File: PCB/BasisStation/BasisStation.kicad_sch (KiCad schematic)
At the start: 1 part, among them U1 ESP32-S3-WROOM-1-N16R8

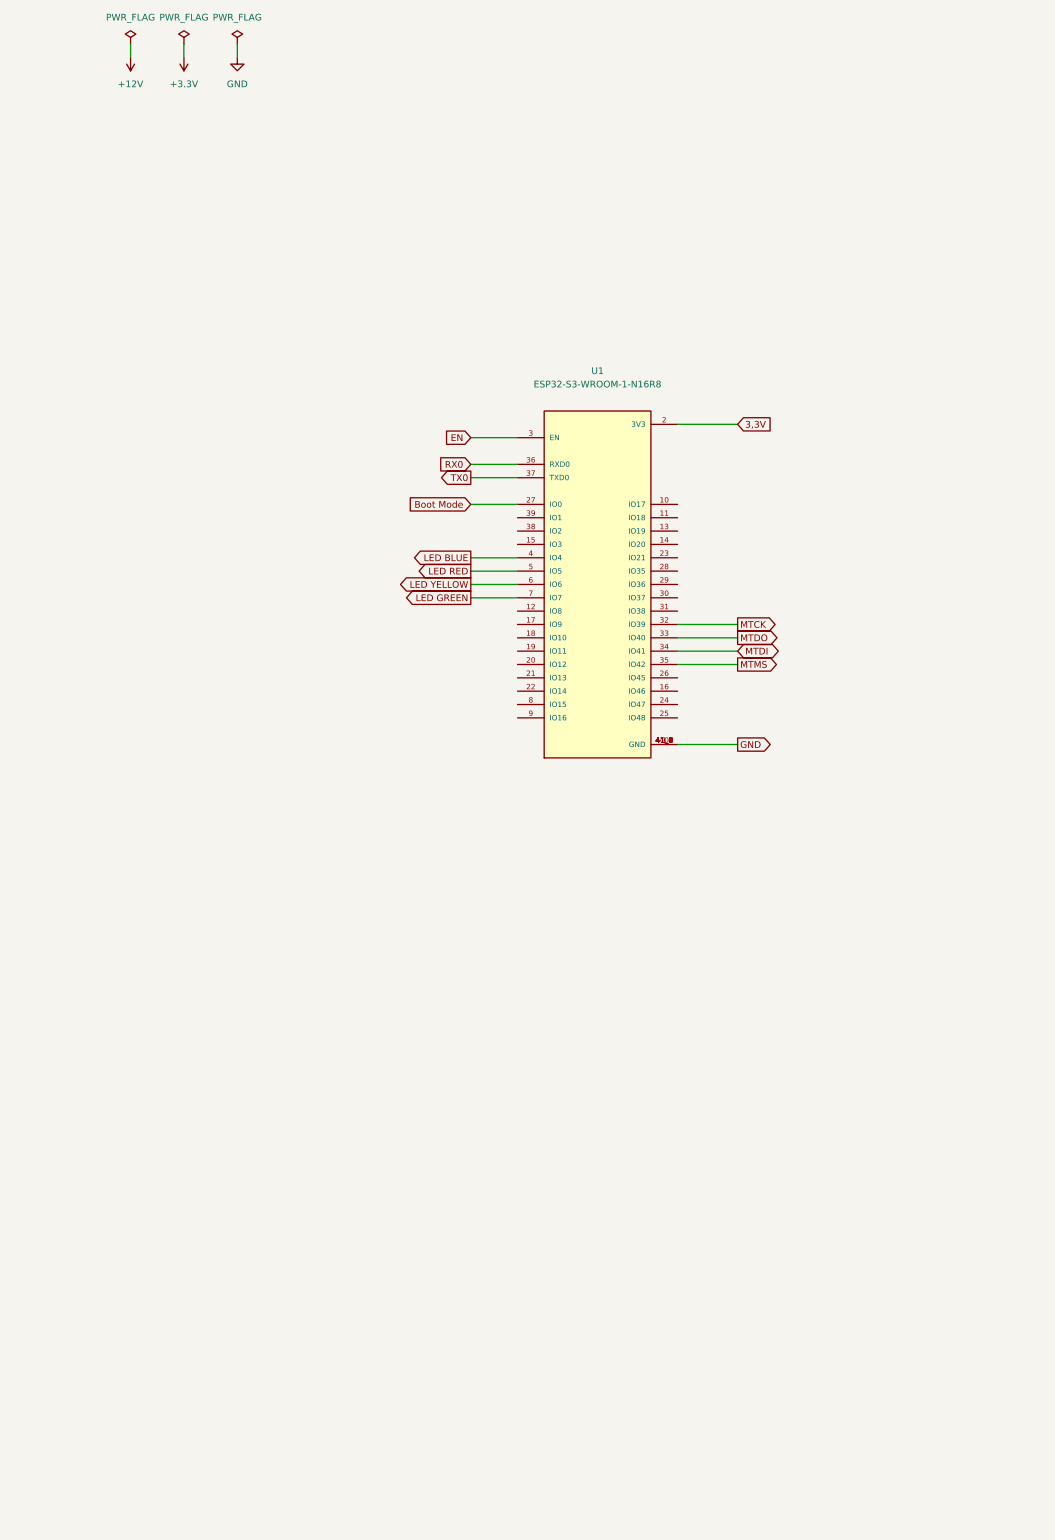
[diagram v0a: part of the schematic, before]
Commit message: ESP32-S3 von der Espressif Library hinzugefügt und Schaltplan angepasst
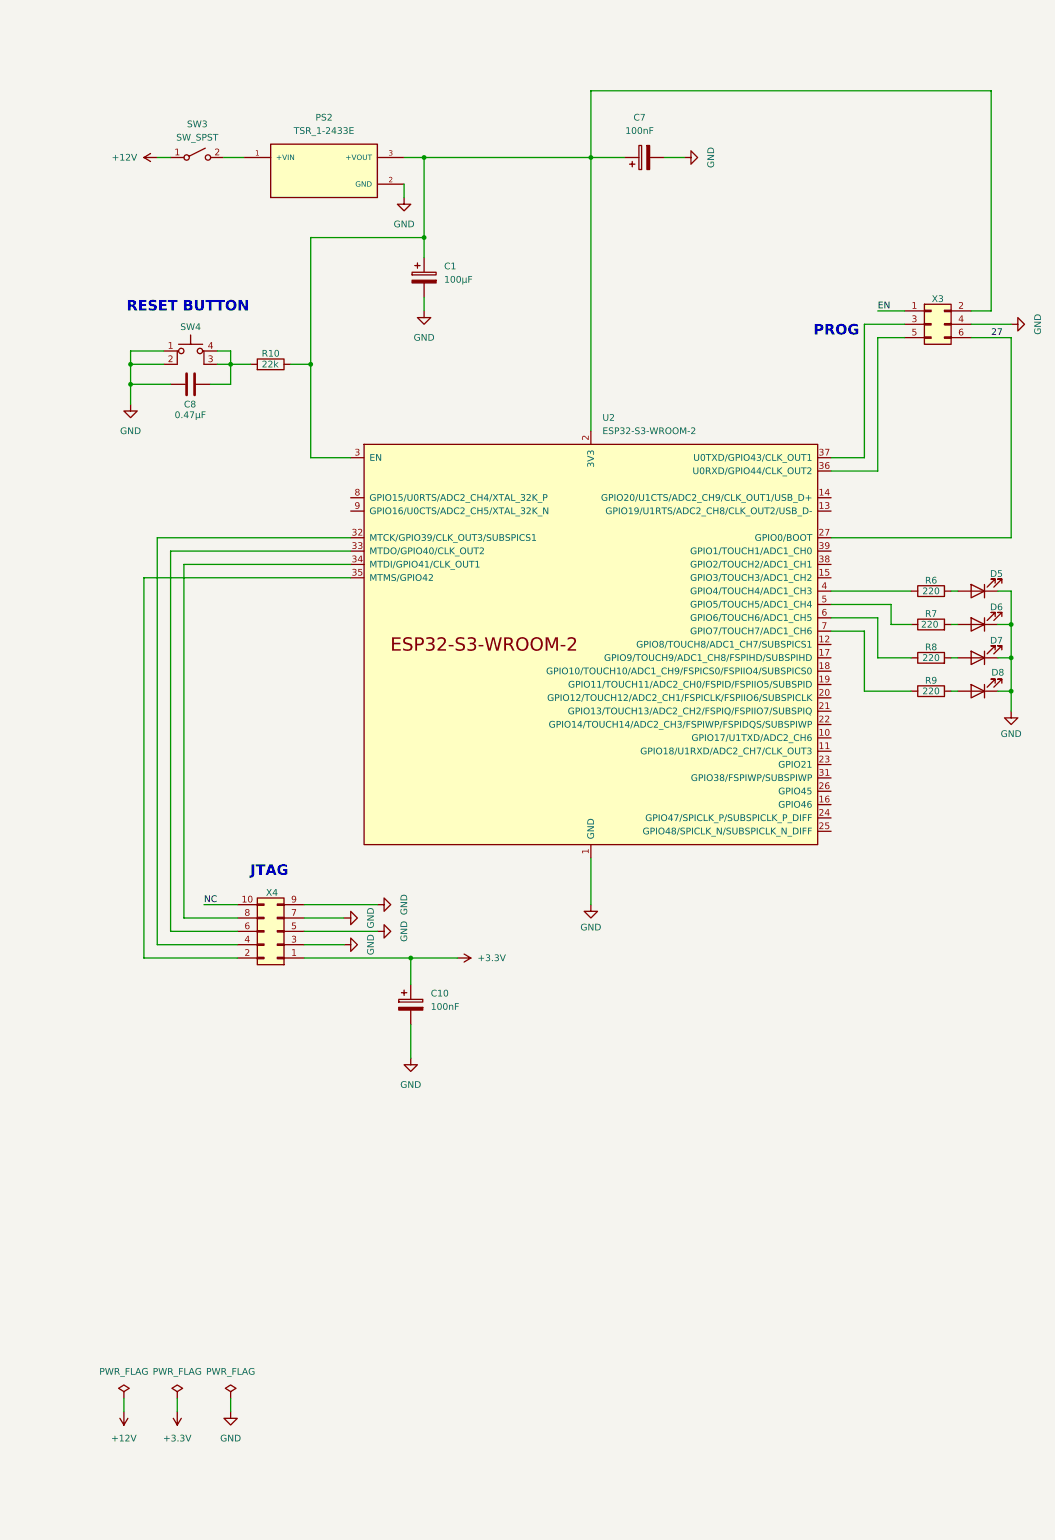
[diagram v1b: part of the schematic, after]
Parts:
- removed U1: ESP32-S3-WROOM-1-N16R8, Template:XCVR_ESP32-S3-WROOM-1-N16R8, symbol ESP32-S3:ESP32-S3-WROOM-1-N16R8
- added C1: 100µF, CUSTOM_Footprint:CAPAE1030X1050N, symbol Device:C_Polarized
- added C10, C7: 100nF, CUSTOM_Footprint:CAPAE1030X1050N, symbol Device:C_Polarized
- added C8: 0.47µF, CUSTOM_Footprint:CAPAE530X565N, symbol Device:C
- added D5, D6, D7, D8: LED, CUSTOM_Footprint:LED-RED-3MM-ROUND, symbol Device:LED
- added PS2: TSR_1-2433E, Template:CONV_TSR_1-2433E, symbol TSR_1-2433E:TSR_1-2433E
- added R10: 22k, Resistor_THT:R_Axial_Power_L60.0mm_W14.0mm_P66.04mm, symbol Device:R
- added R6, R7, R8, R9: 220, Resistor_THT:R_Axial_DIN0207_L6.3mm_D2.5mm_P7.62mm_Horizontal, symbol Device:R
- added SW3: SW_SPST, CUSTOM_Footprint:WUE_SW_471001264143_2_00-3_00_, symbol Switch:SW_SPST
- added SW4: RESET_BUTTON, Button_Switch_THT:SW_PUSH_1P1T_6x3.5mm_H4.3_APEM_MJTP1243, symbol Switch:SW_MEC_5E
- added U2: ESP32-S3-WROOM-2, PCM_Espressif:ESP32-S3-WROOM-2, symbol PCM_Espressif:ESP32-S3-WROOM-2
- added X3: ~, Connector_PinHeader_2.54mm:PinHeader_2x03_P2.54mm_Vertical, symbol Connector_Generic:Conn_02x03_Odd_Even
- added X4: JTAG, CUSTOM_Footprint:WUE_CONNECTOR_SHDR10W64P254_2X5_2036X885X925P, symbol Connector_Generic:Conn_02x05_Odd_Even
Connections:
- net +12V: now also SW3.1 (A)
- net +3.3V: now also C10.1, X4.1 (Pin_1)
- net EN: now also X3.1 (Pin_1)
- net GND: now also C1.2, C10.2, C7.2, C8.1, D5.1 (K), D6.1 (K), D7.1 (K), D8.1 (K), PS2.2 (GND), SW4.1, SW4.2, U2.1 (GND), U2.40 (GND), U2.41 (GND), X3.4 (Pin_4), X4.3 (Pin_3), X4.5 (Pin_5), X4.7 (Pin_7), X4.9 (Pin_9)
- new net: R7.1, U2.5 (GPIO5/TOUCH5/ADC1_CH4)
- new net: D6.2 (A), R7.2
- new net: R8.1, U2.6 (GPIO6/TOUCH6/ADC1_CH5)
- new net: D7.2 (A), R8.2
- new net: C1.1, C7.1, PS2.3 (+VOUT), R10.1, U2.2 (3V3), U2.3 (EN), X3.2 (Pin_2)
- new net: PS2.1 (+VIN), SW3.2 (B)
- new net: U2.35 (MTMS/GPIO42), X4.2 (Pin_2)
- new net: U2.32 (MTCK/GPIO39/CLK_OUT3/SUBSPICS1), X4.4 (Pin_4)
- new net: U2.33 (MTDO/GPIO40/CLK_OUT2), X4.6 (Pin_6)
- new net: U2.34 (MTDI/GPIO41/CLK_OUT1), X4.8 (Pin_8)
- new net: U2.37 (U0TXD/GPIO43/CLK_OUT1), X3.3 (Pin_3)
- new net: U2.36 (U0RXD/GPIO44/CLK_OUT2), X3.5 (Pin_5)
- new net: R6.1, U2.4 (GPIO4/TOUCH4/ADC1_CH3)
- new net: R9.1, U2.7 (GPIO7/TOUCH7/ADC1_CH6)
- new net: D8.2 (A), R9.2
- new net: C8.2, R10.2, SW4.3 (K), SW4.4 (A)
- new net: D5.2 (A), R6.2
- new net 27: U2.27 (GPIO0/BOOT), X3.6 (Pin_6)
- new net NC: X4.10 (Pin_10)
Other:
- note added: "JTAG"
- note added: "PROG"
- note added: "RESET BUTTON"

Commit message: neue Bauteile hinzugefügt
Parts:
- removed PS2: TSR_1-2433E, Template:CONV_TSR_1-2433E, symbol TSR_1-2433E:TSR_1-2433E
- added PS1: TSR1-2433, TSR1-2433:TSR12433, symbol TSR1-2433:TSR1-2433
- R1: renamed from R6; footprint Resistor_THT:R_Axial_DIN0207_L6.3mm_D2.5mm_P7.62mm_Horizontal -> Resistor_THT:R_Axial_DIN0309_L9.0mm_D3.2mm_P12.70mm_Horizontal
- R2: renamed from R7; footprint Resistor_THT:R_Axial_DIN0207_L6.3mm_D2.5mm_P7.62mm_Horizontal -> Resistor_THT:R_Axial_DIN0309_L9.0mm_D3.2mm_P12.70mm_Horizontal
- R3: renamed from R8; footprint Resistor_THT:R_Axial_DIN0207_L6.3mm_D2.5mm_P7.62mm_Horizontal -> Resistor_THT:R_Axial_DIN0309_L9.0mm_D3.2mm_P12.70mm_Horizontal
- R4: renamed from R9; footprint Resistor_THT:R_Axial_DIN0207_L6.3mm_D2.5mm_P7.62mm_Horizontal -> Resistor_THT:R_Axial_DIN0309_L9.0mm_D3.2mm_P12.70mm_Horizontal
- R5: renamed from R10; footprint Resistor_THT:R_Axial_Power_L60.0mm_W14.0mm_P66.04mm -> Resistor_THT:R_Axial_DIN0922_L20.0mm_D9.0mm_P25.40mm_Horizontal
- renumbered C8 to C5, C10 to C6
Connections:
- net GND: now also PS1.2 (GND)
- net at C1.1, C7.1, R5.1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: now also PS1.3 (+VOUT)
- net at SW3.2 (B): now also PS1.1 (+VIN)
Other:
- removed sheet Buttons
- removed sheet JTAG-PROG
- removed sheet LED
- removed sheet Power
- note added: "POWER BUTTON"

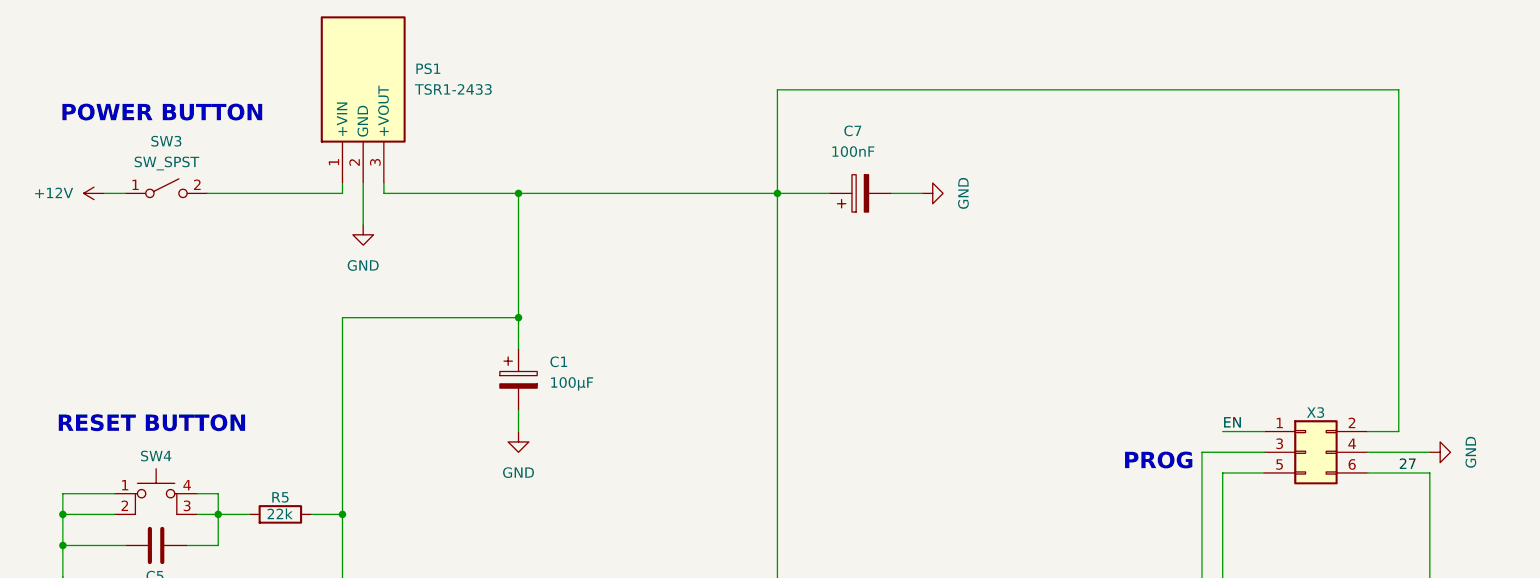
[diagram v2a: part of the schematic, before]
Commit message: Anpassung der Leiterbahnen
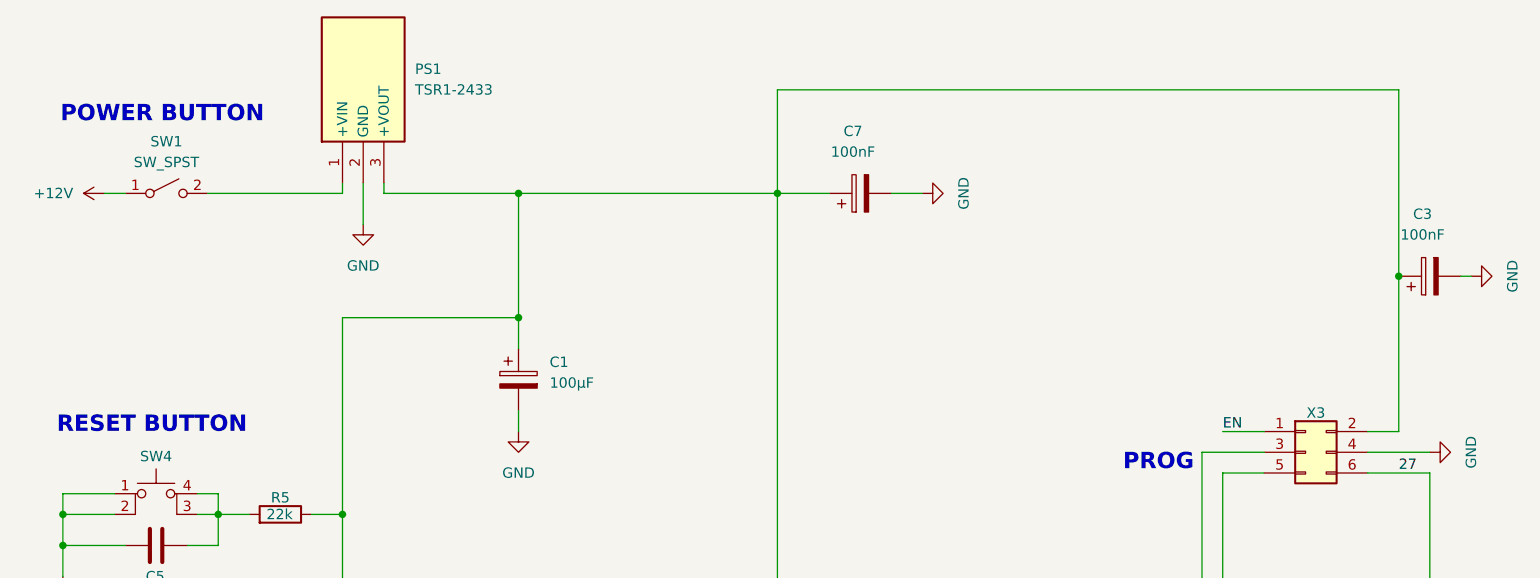
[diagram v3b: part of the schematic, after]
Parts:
- added C3: 100nF, Capacitor_THT:CP_Radial_D6.3mm_P2.50mm, symbol Device:C_Polarized
- C1, C6, C7: footprint CUSTOM_Footprint:CAPAE1030X1050N -> Capacitor_THT:CP_Radial_D6.3mm_P2.50mm
- renumbered SW3 to SW1
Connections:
- net GND: now also C3.2
- net at C1.1, C7.1, PS1.3 (+VOUT)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: now also C3.1
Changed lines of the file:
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@@
+	)
+	(junction
+		(at 181.61 50.8)
+		(diameter 0)
+		(color 0 0 0 0)
 	)
 	(junction
@@
 	(wire
 		(pts
+			(xy 189.23 50.8) (xy 190.5 50.8)
+		)
+		(stroke
+			(width 0)
+			(type default)
+		)
+	)
+	(wire
+		(pts
 			(xy 36.83 83.82) (xy 36.83 80.01)
 		)
@@
 	(wire
 		(pts
+			(xy 181.61 50.8) (xy 181.61 27.94)
+		)
+		(stroke
+			(width 0)
+			(type default)
+		)
+	)
+	(wire
+		(pts
 			(xy 185.42 142.24) (xy 185.42 146.05)
 		)
@@
 	(wire
 		(pts
-			(xy 181.61 69.85) (xy 181.61 27.94)
+			(xy 181.61 69.85) (xy 181.61 50.8)
 		)
 		(stroke
@@
 	)
 	(symbol
+		(lib_id "power:GND")
+		(at 190.5 50.8 90)
+		(unit 1)
+		(exclude_from_sim no)
+		(in_bom yes)
+		(on_board yes)
+		(dnp no)
+		(fields_autoplaced yes)
+		(property "Reference" "#PWR01"
+			(at 196.85 50.8 0)
+			(effects
+				(font
+					(size 1.27 1.27)
+				)
+				(hide yes)
+			)
+		)
+		(property "Value" "GND"
+			(at 195.58 50.8 0)
+			(effects
+				(font
+					(size 1.27 1.27)
+				)
+			)
+		)
+		(property "Footprint" ""
+			(at 190.5 50.8 0)
+			(effects
+				(font
+					(size 1.27 1.27)
+				)
+				(hide yes)
+			)
+		)
+		(property "Datasheet" ""
+			(at 190.5 50.8 0)
+			(effects
+				(font
+					(size 1.27 1.27)
+				)
+				(hide yes)
+			)
+		)
+		(property "Description" "Power symbol creates a global label with name \"GND\" , ground"
+			(at 190.5 50.8 0)
+			(effects
+				(font
+					(size 1.27 1.27)
+				)
+				(hide yes)
+			)
+		)
+		(pin "1"
+		)
+		(instances
+			(project "BasisStation"
+				(path "/cc03a18a-a128-4e00-a998-441923eeacd1"
+					(reference "#PWR01")
+					(unit 1)
+				)
+			)
+		)
+	)
+	(symbol
 		(lib_name "R_1")
 		(lib_id "Device:R")
@@
 			)
 		)
-		(property "Footprint" "CUSTOM_Footprint:CAPAE1030X1050N"
+		(property "Footprint" "Capacitor_THT:CP_Radial_D6.3mm_P2.50mm"
 			(at 119.38 39.6748 0)
 			(effects
@@
 			)
 		)
-		(property "Footprint" "CUSTOM_Footprint:CAPAE1030X1050N"
+		(property "Footprint" "Capacitor_THT:CP_Radial_D6.3mm_P2.50mm"
 			(at 72.0852 205.74 0)
 			(effects
@@
 		(dnp no)
 		(fields_autoplaced yes)
-		(property "Reference" "SW3"
+		(property "Reference" "SW1"
 			(at 30.48 34.29 0)
 			(effects
@@
 			(project "BasisStation"
 				(path "/cc03a18a-a128-4e00-a998-441923eeacd1"
-					(reference "SW3")
+					(reference "SW1")
 					(unit 1)
 				)
@@
 			)
 		)
-		(property "Footprint" "CUSTOM_Footprint:CAPAE1030X1050N"
+		(property "Footprint" "Capacitor_THT:CP_Radial_D6.3mm_P2.50mm"
 			(at 74.6252 67.31 0)
 			(effects
@@
 					(unit 1)
 				)
+			)
+		)
+	)
+	(symbol
+		(lib_id "Device:C_Polarized")
+		(at 185.42 50.8 90)
+		(unit 1)
+		(exclude_from_sim no)
+		(in_bom yes)
+		(on_board yes)
+		(dnp no)
+		(fields_autoplaced yes)
+		(property "Reference" "C3"
+			(at 184.531 43.18 90)
+			(effects
+				(font
+					(size 1.27 1.27)
+				)
+			)
+		)
+		(property "Value" "100nF"
+			(at 184.531 45.72 90)
+			(effects
+				(font
+					(size 1.27 1.27)
+				)
+			)
+		)
+		(property "Footprint" "Capacitor_THT:CP_Radial_D6.3mm_P2.50mm"
+			(at 189.23 49.8348 0)
+			(effects
+				(font
+					(size 1.27 1.27)
+				)
+				(hide yes)
+			)
+		)
+		(property "Datasheet" "chrome-extension://efaidnbmnnnibpcajpcglclefindmkaj/https://www.we-online.com/components/products/datasheet/865060343005.pdf"
+			(at 185.42 50.8 0)
+			(effects
+				(font
+					(size 1.27 1.27)
+				)
+				(hide yes)
+			)
+		)
+		(property "Description" "Polarized capacitor"
+			(at 185.42 50.8 0)
+			(effects
+				(font
+					(size 1.27 1.27)
+				)
+				(hide yes)
+			)
+		)
+		(pin "2"
+		)
+		(pin "1"
+		)
+		(instances
+			(project "BasisStation"
+				(path "/cc03a18a-a128-4e00-a998-441923eeacd1"
+					(reference "C3")
+					(unit 1)
+				)
